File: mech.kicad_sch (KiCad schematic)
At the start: 4 parts

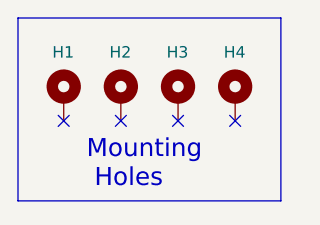
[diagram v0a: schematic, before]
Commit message: Some more decoupling caps and routing optimizations.
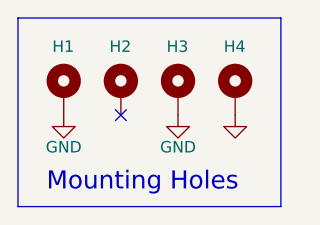
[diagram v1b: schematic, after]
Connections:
- net GND: now reaches H3.1
- net GND: now also H1.1, H4.1
- no-connect marks 4 -> 1
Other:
- moved on the sheet: H1, H2, H3, H4
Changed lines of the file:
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@@
     (rev "1.0")
   )
-  (no_connect (at 69.85 57.785))
-  (no_connect (at 50.8 57.785))
-  (no_connect (at 63.5 57.785))
-  (no_connect (at 57.15 57.785))
-  (polyline (pts (xy 45.72 46.355) (xy 45.72 66.675))
+  (no_connect (at 57.15 57.15))
+  (polyline (pts (xy 45.72 46.355) (xy 45.72 67.31))
     (stroke (width 0) (type default) (color 0 0 0 0))
   )
-  (polyline (pts (xy 74.93 46.355) (xy 74.93 66.675))
+  (polyline (pts (xy 74.93 46.355) (xy 74.93 67.31))
     (stroke (width 0) (type default) (color 0 0 0 0))
   )
@@
     (stroke (width 0) (type default) (color 0 0 0 0))
   )
-  (polyline (pts (xy 74.93 66.675) (xy 45.72 66.675))
+  (polyline (pts (xy 74.93 67.31) (xy 45.72 67.31))
     (stroke (width 0) (type default) (color 0 0 0 0))
   )
-  (text "Mounting\n Holes" (at 53.34 65.405 0)
+  (text "Mounting Holes" (at 48.895 65.786 0)
     (effects (font (size 2 2)) (justify left bottom))
   )
-  (symbol (lib_id "Mechanical:MountingHole_Pad") (at 63.5 55.245 0) (unit 1)
-    (in_bom no) (on_board yes)
-    (property "Reference" "H3" (id 0) (at 62.23 50.165 0)
-      (effects (font (size 1.27 1.27)) (justify left))
-    )
-    (property "Value" "MountingHole_Pad" (id 1) (at 66.04 55.2449 0)
-      (effects (font (size 1.27 1.27)) (justify left) hide)
-    )
-    (property "Footprint" "MountingHole:MountingHole_3.2mm_M3_ISO14580_Pad" (id 2) (at 63.5 55.245 0)
+  (symbol (lib_id "power:GND") (at 63.5 57.15 0) (unit 1)
+    (in_bom yes) (on_board yes)
+    (property "Reference" "#PWR0109" (id 0) (at 63.5 63.5 0)
       (effects (font (size 1.27 1.27)) hide)
     )
-    (property "Datasheet" "~" (id 3) (at 63.5 55.245 0)
+    (property "Value" "GND" (id 1) (at 63.5 60.706 0))
+    (property "Footprint" "" (id 2) (at 63.5 57.15 0)
+      (effects (font (size 1.27 1.27)) hide)
+    )
+    (property "Datasheet" "" (id 3) (at 63.5 57.15 0)
       (effects (font (size 1.27 1.27)) hide)
     )
     (pin "1")
   )
-  (symbol (lib_id "Mechanical:MountingHole_Pad") (at 57.15 55.245 0) (unit 1)
+  (symbol (lib_id "Mechanical:MountingHole_Pad") (at 63.5 54.61 0) (unit 1)
     (in_bom no) (on_board yes)
-    (property "Reference" "H2" (id 0) (at 55.88 50.165 0)
+    (property "Reference" "H3" (id 0) (at 62.23 49.53 0)
       (effects (font (size 1.27 1.27)) (justify left))
     )
-    (property "Value" "MountingHole_Pad" (id 1) (at 59.69 55.2449 0)
+    (property "Value" "MountingHole_Pad" (id 1) (at 66.04 54.6099 0)
       (effects (font (size 1.27 1.27)) (justify left) hide)
     )
-    (property "Footprint" "MountingHole:MountingHole_3.2mm_M3_ISO14580_Pad" (id 2) (at 57.15 55.245 0)
+    (property "Footprint" "MountingHole:MountingHole_3.2mm_M3_ISO14580_Pad" (id 2) (at 63.5 54.61 0)
       (effects (font (size 1.27 1.27)) hide)
     )
-    (property "Datasheet" "~" (id 3) (at 57.15 55.245 0)
+    (property "Datasheet" "~" (id 3) (at 63.5 54.61 0)
       (effects (font (size 1.27 1.27)) hide)
     )
     (pin "1")
   )
-  (symbol (lib_id "Mechanical:MountingHole_Pad") (at 69.85 55.245 0) (unit 1)
-    (in_bom no) (on_board yes)
-    (property "Reference" "H4" (id 0) (at 68.58 50.165 0)
-      (effects (font (size 1.27 1.27)) (justify left))
-    )
-    (property "Value" "MountingHole_Pad" (id 1) (at 72.39 55.2449 0)
-      (effects (font (size 1.27 1.27)) (justify left) hide)
-    )
-    (property "Footprint" "MountingHole:MountingHole_3.2mm_M3_ISO14580_Pad" (id 2) (at 69.85 55.245 0)
+  (symbol (lib_id "power:GND") (at 50.8 57.15 0) (unit 1)
+    (in_bom yes) (on_board yes)
+    (property "Reference" "#PWR0106" (id 0) (at 50.8 63.5 0)
       (effects (font (size 1.27 1.27)) hide)
     )
-    (property "Datasheet" "~" (id 3) (at 69.85 55.245 0)
+    (property "Value" "GND" (id 1) (at 50.8 60.706 0))
+    (property "Footprint" "" (id 2) (at 50.8 57.15 0)
+      (effects (font (size 1.27 1.27)) hide)
+    )
+    (property "Datasheet" "" (id 3) (at 50.8 57.15 0)
       (effects (font (size 1.27 1.27)) hide)
     )
     (pin "1")
   )
-  (symbol (lib_id "Mechanical:MountingHole_Pad") (at 50.8 55.245 0) (unit 1)
+  (symbol (lib_id "Mechanical:MountingHole_Pad") (at 57.15 54.61 0) (unit 1)
     (in_bom no) (on_board yes)
-    (property "Reference" "H1" (id 0) (at 49.53 50.165 0)
+    (property "Reference" "H2" (id 0) (at 55.88 49.53 0)
       (effects (font (size 1.27 1.27)) (justify left))
     )
-    (property "Value" "MountingHole_Pad" (id 1) (at 53.34 55.2449 0)
+    (property "Value" "MountingHole_Pad" (id 1) (at 59.69 54.6099 0)
       (effects (font (size 1.27 1.27)) (justify left) hide)
     )
-    (property "Footprint" "MountingHole:MountingHole_3.2mm_M3_ISO14580_Pad" (id 2) (at 50.8 55.245 0)
+    (property "Footprint" "MountingHole:MountingHole_3.2mm_M3_ISO14580_Pad" (id 2) (at 57.15 54.61 0)
       (effects (font (size 1.27 1.27)) hide)
     )
-    (property "Datasheet" "~" (id 3) (at 50.8 55.245 0)
+    (property "Datasheet" "~" (id 3) (at 57.15 54.61 0)
       (effects (font (size 1.27 1.27)) hide)
     )
+    (pin "1")
+  )
+  (symbol (lib_id "Mechanical:MountingHole_Pad") (at 69.85 54.61 0) (unit 1)
+    (in_bom no) (on_board yes)
+    (property "Reference" "H4" (id 0) (at 68.58 49.53 0)
+      (effects (font (size 1.27 1.27)) (justify left))
+    )
+    (property "Value" "MountingHole_Pad" (id 1) (at 72.39 54.6099 0)
+      (effects (font (size 1.27 1.27)) (justify left) hide)
+    )
+    (property "Footprint" "MountingHole:MountingHole_3.2mm_M3_ISO14580_Pad" (id 2) (at 69.85 54.61 0)
+      (effects (font (size 1.27 1.27)) hide)
+    )
+    (property "Datasheet" "~" (id 3) (at 69.85 54.61 0)
+      (effects (font (size 1.27 1.27)) hide)
+    )
+    (pin "1")
+  )
+  (symbol (lib_id "Mechanical:MountingHole_Pad") (at 50.8 54.61 0) (unit 1)
+    (in_bom no) (on_board yes)
+    (property "Reference" "H1" (id 0) (at 49.53 49.53 0)
+      (effects (font (size 1.27 1.27)) (justify left))
+    )
+    (property "Value" "MountingHole_Pad" (id 1) (at 53.34 54.6099 0)
+      (effects (font (size 1.27 1.27)) (justify left) hide)
+    )
+    (property "Footprint" "MountingHole:MountingHole_3.2mm_M3_ISO14580_Pad" (id 2) (at 50.8 54.61 0)
+      (effects (font (size 1.27 1.27)) hide)
+    )
+    (property "Datasheet" "~" (id 3) (at 50.8 54.61 0)
+      (effects (font (size 1.27 1.27)) hide)
+    )
+    (pin "1")
+  )
+  (symbol (lib_id "power:GND") (at 69.85 57.15 0) (unit 1)
+    (in_bom yes) (on_board yes)
+    (property "Reference" "#PWR0108" (id 0) (at 69.85 63.5 0)
+      (effects (font (size 1.27 1.27)) hide)
+    )
+    (property "Value" "" (id 1) (at 69.85 60.706 0))
+    (property "Footprint" "" (id 2) (at 69.85 57.15 0)
+      (effects (font (size 1.27 1.27)) hide)
+    )
+    (property "Datasheet" "" (id 3) (at 69.85 57.15 0)
+      (effects (font (size 1.27 1.27)) hide)
+    )

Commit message: Lots of changes and errors fixed. Updated vanity images.
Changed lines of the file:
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@@
       (effects (font (size 1.27 1.27)) hide)
     )
-    (property "Value" "" (id 1) (at 69.85 60.706 0))
+    (property "Value" "GND" (id 1) (at 69.85 60.706 0))
     (property "Footprint" "" (id 2) (at 69.85 57.15 0)
       (effects (font (size 1.27 1.27)) hide)

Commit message: Tweaks and JLCPCB LCSC field name changes.
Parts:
- H1, H2, H3, H4: value MountingHole_Pad -> (none); footprint MountingHole:MountingHole_3.2mm_M3_ISO14580_Pad -> (none)
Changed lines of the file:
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@@
       (effects (font (size 1.27 1.27)) (justify left))
     )
-    (property "Value" "MountingHole_Pad" (id 1) (at 66.04 54.6099 0)
+    (property "Value" "" (id 1) (at 66.04 54.6099 0)
       (effects (font (size 1.27 1.27)) (justify left) hide)
     )
-    (property "Footprint" "MountingHole:MountingHole_3.2mm_M3_ISO14580_Pad" (id 2) (at 63.5 54.61 0)
+    (property "Footprint" "" (id 2) (at 63.5 54.61 0)
       (effects (font (size 1.27 1.27)) hide)
     )
@@
       (effects (font (size 1.27 1.27)) (justify left))
     )
-    (property "Value" "MountingHole_Pad" (id 1) (at 59.69 54.6099 0)
+    (property "Value" "" (id 1) (at 59.69 54.6099 0)
       (effects (font (size 1.27 1.27)) (justify left) hide)
     )
-    (property "Footprint" "MountingHole:MountingHole_3.2mm_M3_ISO14580_Pad" (id 2) (at 57.15 54.61 0)
+    (property "Footprint" "" (id 2) (at 57.15 54.61 0)
       (effects (font (size 1.27 1.27)) hide)
     )
@@
       (effects (font (size 1.27 1.27)) (justify left))
     )
-    (property "Value" "MountingHole_Pad" (id 1) (at 72.39 54.6099 0)
+    (property "Value" "" (id 1) (at 72.39 54.6099 0)
       (effects (font (size 1.27 1.27)) (justify left) hide)
     )
-    (property "Footprint" "MountingHole:MountingHole_3.2mm_M3_ISO14580_Pad" (id 2) (at 69.85 54.61 0)
+    (property "Footprint" "" (id 2) (at 69.85 54.61 0)
       (effects (font (size 1.27 1.27)) hide)
     )
@@
       (effects (font (size 1.27 1.27)) (justify left))
     )
-    (property "Value" "MountingHole_Pad" (id 1) (at 53.34 54.6099 0)
+    (property "Value" "" (id 1) (at 53.34 54.6099 0)
       (effects (font (size 1.27 1.27)) (justify left) hide)
     )
-    (property "Footprint" "MountingHole:MountingHole_3.2mm_M3_ISO14580_Pad" (id 2) (at 50.8 54.61 0)
+    (property "Footprint" "" (id 2) (at 50.8 54.61 0)
       (effects (font (size 1.27 1.27)) hide)
     )

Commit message: I'm soooo done with this board! :/
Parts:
- H1, H2, H3, H4: value (none) -> MountingHole_Pad; footprint (none) -> MountingHole:MountingHole_3.2mm_M3_ISO14580_Pad; JLCMFR# (none) -> DNI
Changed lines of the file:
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@@
       (effects (font (size 1.27 1.27)) (justify left))
     )
-    (property "Value" "" (id 1) (at 66.04 54.6099 0)
+    (property "Value" "MountingHole_Pad" (id 1) (at 66.04 54.6099 0)
       (effects (font (size 1.27 1.27)) (justify left) hide)
     )
-    (property "Footprint" "" (id 2) (at 63.5 54.61 0)
+    (property "Footprint" "MountingHole:MountingHole_3.2mm_M3_ISO14580_Pad" (id 2) (at 63.5 54.61 0)
       (effects (font (size 1.27 1.27)) hide)
     )
     (property "Datasheet" "~" (id 3) (at 63.5 54.61 0)
+      (effects (font (size 1.27 1.27)) hide)
+    )
+    (property "JLCPART" "" (id 4) (at 63.5 54.61 0)
+      (effects (font (size 1.27 1.27)) hide)
+    )
+    (property "JLCMFR#" "DNI" (id 5) (at 63.5 54.61 0)
       (effects (font (size 1.27 1.27)) hide)
     )
@@
       (effects (font (size 1.27 1.27)) (justify left))
     )
-    (property "Value" "" (id 1) (at 59.69 54.6099 0)
+    (property "Value" "MountingHole_Pad" (id 1) (at 59.69 54.6099 0)
       (effects (font (size 1.27 1.27)) (justify left) hide)
     )
-    (property "Footprint" "" (id 2) (at 57.15 54.61 0)
+    (property "Footprint" "MountingHole:MountingHole_3.2mm_M3_ISO14580_Pad" (id 2) (at 57.15 54.61 0)
       (effects (font (size 1.27 1.27)) hide)
     )
     (property "Datasheet" "~" (id 3) (at 57.15 54.61 0)
+      (effects (font (size 1.27 1.27)) hide)
+    )
+    (property "JLCMFR#" "DNI" (id 5) (at 57.15 54.61 0)
       (effects (font (size 1.27 1.27)) hide)
     )
@@
       (effects (font (size 1.27 1.27)) (justify left))
     )
-    (property "Value" "" (id 1) (at 72.39 54.6099 0)
+    (property "Value" "MountingHole_Pad" (id 1) (at 72.39 54.6099 0)
       (effects (font (size 1.27 1.27)) (justify left) hide)
     )
-    (property "Footprint" "" (id 2) (at 69.85 54.61 0)
+    (property "Footprint" "MountingHole:MountingHole_3.2mm_M3_ISO14580_Pad" (id 2) (at 69.85 54.61 0)
       (effects (font (size 1.27 1.27)) hide)
     )
     (property "Datasheet" "~" (id 3) (at 69.85 54.61 0)
+      (effects (font (size 1.27 1.27)) hide)
+    )
+    (property "JLCPART" "" (id 4) (at 69.85 54.61 0)
+      (effects (font (size 1.27 1.27)) hide)
+    )
+    (property "JLCMFR#" "DNI" (id 5) (at 69.85 54.61 0)
       (effects (font (size 1.27 1.27)) hide)
     )
@@
       (effects (font (size 1.27 1.27)) (justify left))
     )
-    (property "Value" "" (id 1) (at 53.34 54.6099 0)
+    (property "Value" "MountingHole_Pad" (id 1) (at 53.34 54.6099 0)
       (effects (font (size 1.27 1.27)) (justify left) hide)
     )
-    (property "Footprint" "" (id 2) (at 50.8 54.61 0)
+    (property "Footprint" "MountingHole:MountingHole_3.2mm_M3_ISO14580_Pad" (id 2) (at 50.8 54.61 0)
       (effects (font (size 1.27 1.27)) hide)
     )
@@
       (effects (font (size 1.27 1.27)) hide)
     )
+    (property "JLCMFR#" "DNI" (id 5) (at 50.8 54.61 0)
+      (effects (font (size 1.27 1.27)) hide)
+    )
